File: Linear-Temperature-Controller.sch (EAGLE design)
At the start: 67 parts, among them IC1 LM393D, IC3 AD5624R, IC4 AD5262, IC5 OP27, T1 MMBT3904, T2 MMBT3904

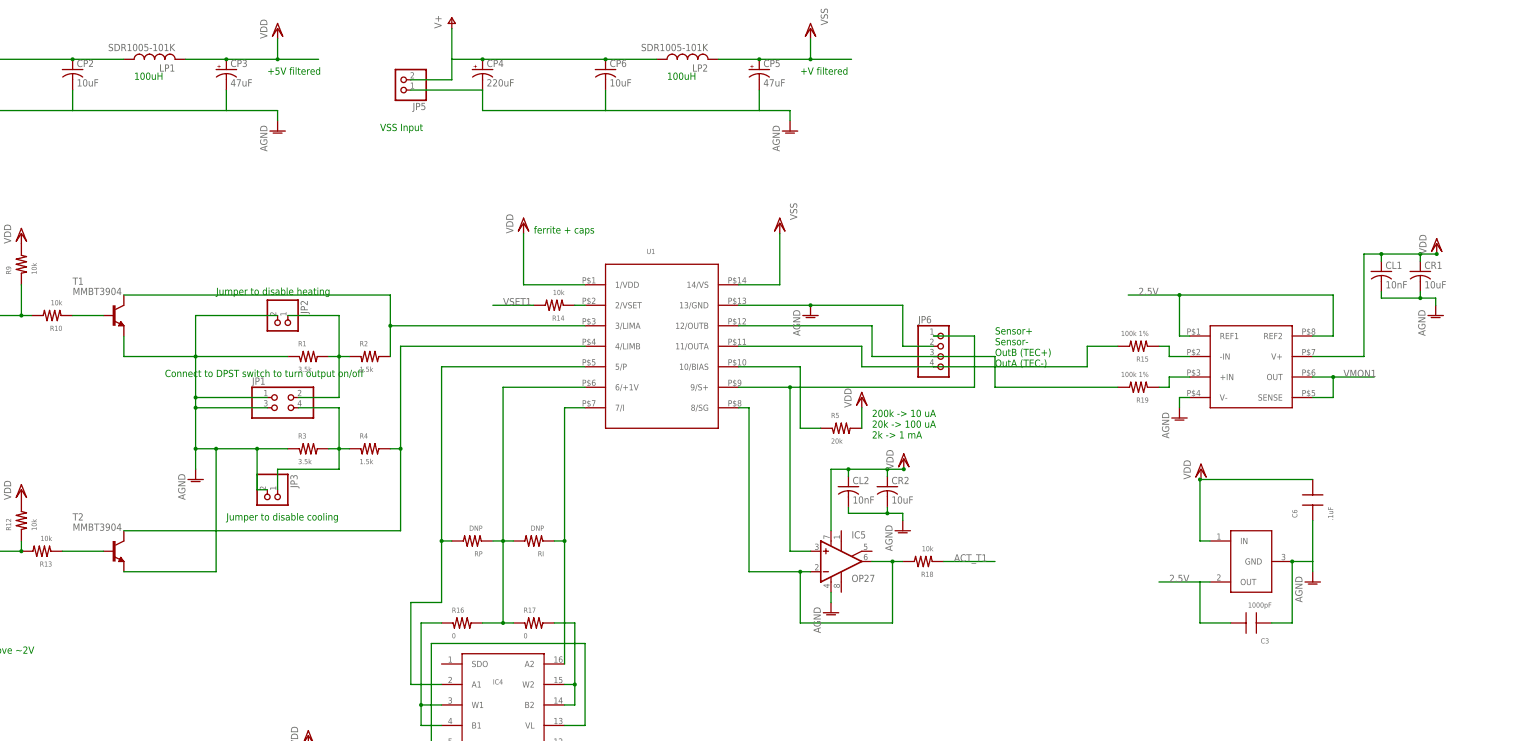
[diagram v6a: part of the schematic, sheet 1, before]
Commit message: Start laying out board and update schematic
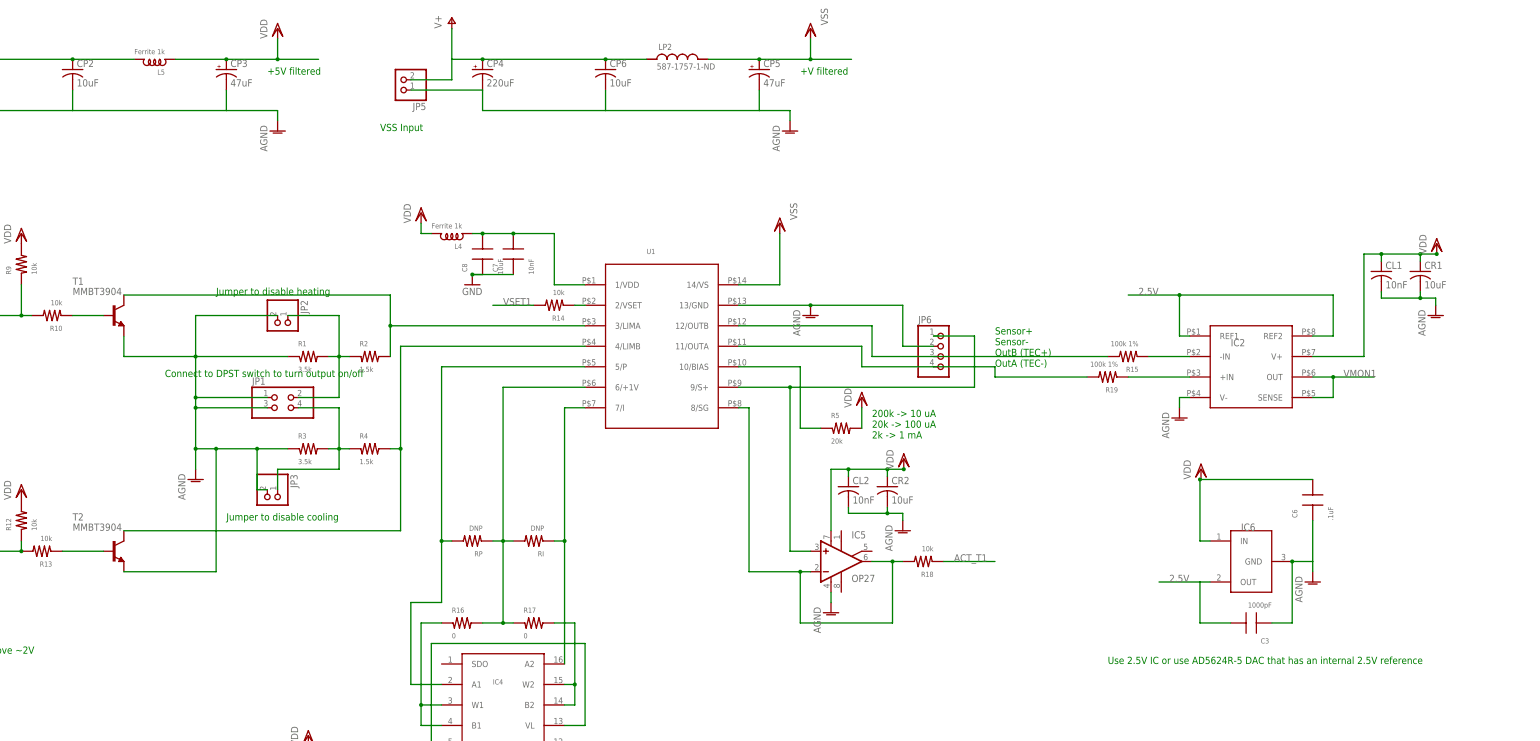
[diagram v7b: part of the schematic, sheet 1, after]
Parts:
- removed LP1: SDR1005-101K, misc-ics:SDR1005-101K
- added C7: 10nF, rlc-jqi:CAP0805
- added C8: 10uF, rlc-jqi:CAP0805
- added L4, L5: Ferrite 1k, rlc-jqi:INDUCTOR-0805
- C27, C4: device rlc-jqi:CAP0603 -> rlc-jqi:CAP0805
- LP2: value SDR1005-101K -> 587-1757-1-ND; device misc-ics:SDR1005-101K -> jqi_passives:L_FERRITE_SMD
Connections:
- removed net N$29: U$1.12/MISO
- new net N$26: C7.P$2, C8.P$2, L4.P$1, U1.1/VDD
- new net N$99: U$1.23/A9/T/PWM
- net +5V: now also L5.P$2; no longer LP1.1
- net ACT_T1: now also U$1.22/A8/T/PWM; no longer U$1.14/A0
- net ACT_T2: now also U$1.20/A6/PWM; no longer U$1.16/A2/T
- net ACT_T4: now also U$1.16/A2/T; no longer U$1.20/A6/PWM
- net CS_DAC: now also U$1.14/A0; no longer U$1.3/CAN-TX/PWM
- net CS_LCD: now also U$1.5/PWM; no longer U$1.0/RX1/T
- net CS_POT1: now also U$1.8/TX3; no longer U$1.4/CAN-RX-PWM
- net CS_POT2: now also U$1.9/RX2/PWM; no longer U$1.5/PWM
- net CS_POT3: now also U$1.10/TX2/PWM; no longer U$1.6/PWM
- net CS_POT4: now also U$1.12/MISO; no longer U$1.7/RX3
- net DGND: now also C7.P$1, C8.P$1
- net ENC_A1: now also U$1.2; no longer U$1.10/TX2/PWM
- net ENC_A2: now also U$1.4/CAN-RX-PWM; no longer U$1.23/A9/T/PWM
- net ENC_B1: now also U$1.1/TX1/T; no longer U$1.9/RX2/PWM
- net ENC_B2: now also U$1.3/CAN-TX/PWM; no longer U$1.22/A8/T/PWM
- net ENC_SW1: now also U$1.0/RX1/T; no longer U$1.8/TX3
- net N$21: now also R15.P$2; no longer R19.P$2
- net N$22: now also R19.P$2; no longer R15.P$2
- net RST_LCD: now also U$1.7/RX3; no longer U$1.2
- net RS_LCD: now also U$1.6/PWM; no longer U$1.1/TX1/T
- net VDD: now also L4.P$2, L5.P$1; no longer LP1.2, U1.1/VDD
- net VMON1: now also U$1.21/A7/PWM; no longer U$1.15/A1/T
- net VMON2: now also U$1.19/A5/T/SCL0; no longer U$1.17/A3/T
- net VMON3: now also U$1.17/A3/T; no longer U$1.19/A5/T/SCL0
- net VMON4: now also U$1.15/A1/T; no longer U$1.21/A7/PWM
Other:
- note added: "Use 2.5V IC or use AD5624R-5 DAC that has an internal 2.5V reference"
- note removed: "100uH"
- note removed: "Ferrite bead to decouple pwr supply"
- note removed: "ferrite + caps"
- moved on the sheet: R15, R19

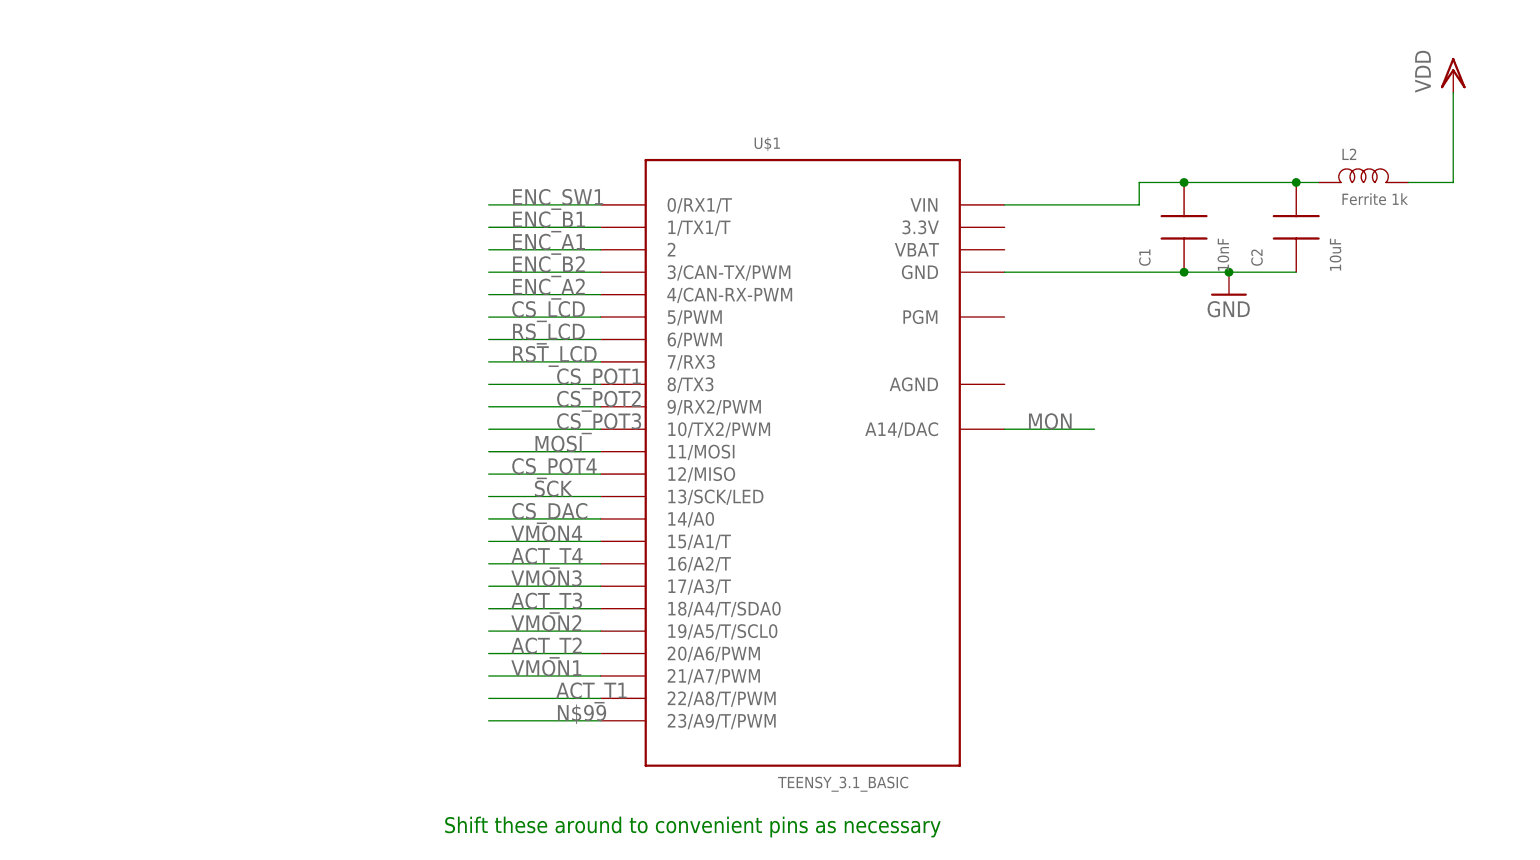
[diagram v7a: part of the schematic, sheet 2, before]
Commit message: Progress...
Added voltage divider to Teensy analog inputs, added a couple extra
teensy channels, layout progress
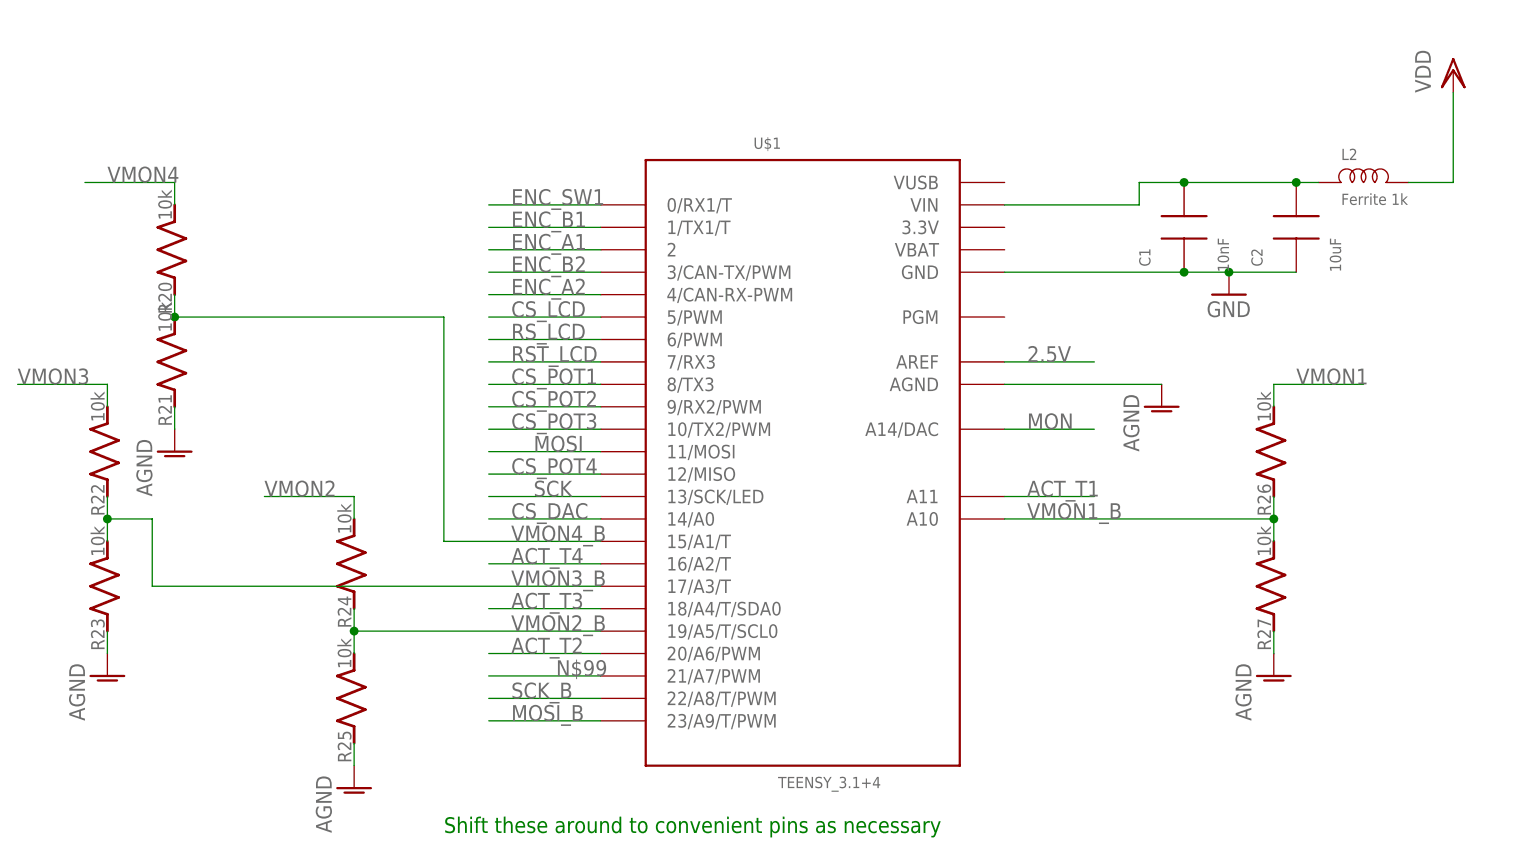
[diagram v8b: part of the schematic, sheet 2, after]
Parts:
- added R20, R21, R22, R23, R24, R25, R26, R27: 10k, jqi_passives:R_SMDR0805
- U$1: value TEENSY_3.1_BASIC -> TEENSY_3.1+4; device mcu-accessories:TEENSY_3.1_BASIC -> mcu-accessories:TEENSY_3.1+4
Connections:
- net N$21 renamed OUTB
- net N$22 renamed OUTA
- new net GND: IC4.VSS
- new net MOSI_B: IC4.SDI, U$1.23/A9/T/PWM
- new net SCK_B: IC4.CLK, U$1.22/A8/T/PWM
- new net VMON1_B: R26.1, R27.2, U$1.A10
- new net VMON2_B: R24.1, R25.2, U$1.19/A5/T/SCL0
- new net VMON3_B: R22.1, R23.2, U$1.17/A3/T
- new net VMON4_B: R20.1, R21.2, U$1.15/A1/T
- net 2.5V: now also U$1.AREF
- net ACT_T1: now also U$1.A11; no longer U$1.22/A8/T/PWM
- net AGND: now also C7.P$1, C8.P$1, R21.1, R23.1, R25.1, R27.1, U$1.AGND; no longer IC4.VSS
- net DGND: no longer C7.P$1, C8.P$1
- net MOSI: no longer IC4.SDI
- net N$99: now also U$1.21/A7/PWM; no longer U$1.23/A9/T/PWM
- net SCK: no longer IC4.CLK
- net VMON1: now also R26.2; no longer U$1.21/A7/PWM
- net VMON2: now also R24.2; no longer U$1.19/A5/T/SCL0
- net VMON3: now also R22.2; no longer U$1.17/A3/T
- net VMON4: now also R20.2; no longer U$1.15/A1/T
